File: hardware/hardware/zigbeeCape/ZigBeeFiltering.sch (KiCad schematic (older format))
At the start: 33 parts, among them U2 0.8Ghz_and_2.4GHz_Filter, U3 SMA_Antenna

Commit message: Completed BOM except unlabled DNM parts, labled in red. Completed footprint association except onboard antenae
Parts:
- AE1: footprint Connector_Coaxial:SMA_Amphenol_132134-16_Vertical -> (none)
- L10, L13, L3, L4, L7: footprint (none) -> Inductor_SMD:L_0402_1005Metric_Pad0.77x0.64mm_HandSolder
- L11, L12, L14, L5, L6, L8, L9: footprint (none) -> Inductor_SMD:L_0603_1608Metric_Pad1.05x0.95mm_HandSolder
- L2: footprint (none) -> Inductor_SMD:L_0805_2012Metric_Pad1.15x1.40mm_HandSolder
- U2: footprint (none) -> zigbeeCape:DPX252690DT-5032B1
- U3: footprint (none) -> Connector_Coaxial:SMA_Amphenol_132134-16_Vertical
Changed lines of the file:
@@
 F 0 "L5" H 2253 4946 50  0000 L CNN
 F 1 "3.9nH" H 2253 4855 50  0000 L CNN
-F 2 "" H 2200 4900 50  0001 C CNN
+F 2 "Inductor_SMD:L_0603_1608Metric_Pad1.05x0.95mm_HandSolder" H 2200 4900 50  0001 C CNN
 F 3 "~" H 2200 4900 50  0001 C CNN
 	1    2200 4900
@@
 F 0 "L6" H 2253 5346 50  0000 L CNN
 F 1 "3.9nH" H 2253 5255 50  0000 L CNN
-F 2 "" H 2200 5300 50  0001 C CNN
+F 2 "Inductor_SMD:L_0603_1608Metric_Pad1.05x0.95mm_HandSolder" H 2200 5300 50  0001 C CNN
 F 3 "~" H 2200 5300 50  0001 C CNN
 	1    2200 5300
@@
 F 0 "L9" H 3053 4696 50  0000 L CNN
 F 1 "10nH" H 3053 4605 50  0000 L CNN
-F 2 "" H 3000 4650 50  0001 C CNN
+F 2 "Inductor_SMD:L_0603_1608Metric_Pad1.05x0.95mm_HandSolder" H 3000 4650 50  0001 C CNN
 F 3 "~" H 3000 4650 50  0001 C CNN
 	1    3000 4650
@@
 F 0 "L12" H 4603 5146 50  0000 L CNN
 F 1 "9.1nH" H 4603 5055 50  0000 L CNN
-F 2 "" H 4550 5100 50  0001 C CNN
+F 2 "Inductor_SMD:L_0603_1608Metric_Pad1.05x0.95mm_HandSolder" H 4550 5100 50  0001 C CNN
 F 3 "~" H 4550 5100 50  0001 C CNN
 	1    4550 5100
@@
 F 0 "L11" H 3453 5346 50  0000 L CNN
 F 1 "10nH" H 3453 5255 50  0000 L CNN
-F 2 "" H 3400 5300 50  0001 C CNN
+F 2 "Inductor_SMD:L_0603_1608Metric_Pad1.05x0.95mm_HandSolder" H 3400 5300 50  0001 C CNN
 F 3 "~" H 3400 5300 50  0001 C CNN
 	1    3400 5300
@@
 F 0 "L8" H 2903 5146 50  0000 L CNN
 F 1 "22nH" H 2903 5055 50  0000 L CNN
-F 2 "" H 2850 5100 50  0001 C CNN
+F 2 "Inductor_SMD:L_0603_1608Metric_Pad1.05x0.95mm_HandSolder" H 2850 5100 50  0001 C CNN
 F 3 "~" H 2850 5100 50  0001 C CNN
 	1    2850 5100
@@
 F 0 "U3" H 7800 3815 50  0000 C CNN
 F 1 "SMA_Antenna" H 7800 3724 50  0000 C CNN
-F 2 "" H 7800 3000 50  0001 C CNN
+F 2 "Connector_Coaxial:SMA_Amphenol_132134-16_Vertical" H 7800 3000 50  0001 C CNN
 F 3 "" H 7800 3000 50  0001 C CNN
 	1    7800 3450
@@
 F 0 "L7" H 3403 3246 50  0000 L CNN
 F 1 "2nH" H 3403 3155 50  0000 L CNN
-F 2 "" H 3350 3200 50  0001 C CNN
+F 2 "Inductor_SMD:L_0402_1005Metric_Pad0.77x0.64mm_HandSolder" H 3350 3200 50  0001 C CNN
 F 3 "~" H 3350 3200 50  0001 C CNN
 	1    3350 3200
@@
 F 0 "L10" H 4103 3246 50  0000 L CNN
 F 1 "2nH" H 4103 3155 50  0000 L CNN
-F 2 "" H 4050 3200 50  0001 C CNN
+F 2 "Inductor_SMD:L_0402_1005Metric_Pad0.77x0.64mm_HandSolder" H 4050 3200 50  0001 C CNN
 F 3 "~" H 4050 3200 50  0001 C CNN
 	1    4050 3200
@@
 F 0 "L3" H 2553 2746 50  0000 L CNN
 F 1 "2.4nH" H 2553 2655 50  0000 L CNN
-F 2 "" H 2500 2700 50  0001 C CNN
+F 2 "Inductor_SMD:L_0402_1005Metric_Pad0.77x0.64mm_HandSolder" H 2500 2700 50  0001 C CNN
 F 3 "~" H 2500 2700 50  0001 C CNN
 	1    2500 2700
@@
 F 0 "L4" H 2953 3546 50  0000 L CNN
 F 1 "2.4nH" H 2953 3455 50  0000 L CNN
-F 2 "" H 2900 3500 50  0001 C CNN
+F 2 "Inductor_SMD:L_0402_1005Metric_Pad0.77x0.64mm_HandSolder" H 2900 3500 50  0001 C CNN
 F 3 "~" H 2900 3500 50  0001 C CNN
 	1    2900 3500
@@
 F 0 "L2" H 2353 3296 50  0000 L CNN
 F 1 "15nH" H 2353 3205 50  0000 L CNN
-F 2 "" H 2300 3250 50  0001 C CNN
+F 2 "Inductor_SMD:L_0805_2012Metric_Pad1.15x1.40mm_HandSolder" H 2300 3250 50  0001 C CNN
 F 3 "~" H 2300 3250 50  0001 C CNN
 	1    2300 3250
@@
 F 0 "L13" V 8390 4250 50  0000 C CNN
 F 1 "3.3nH" V 8299 4250 50  0000 C CNN
-F 2 "" H 8200 4250 50  0001 C CNN
+F 2 "Inductor_SMD:L_0402_1005Metric_Pad0.77x0.64mm_HandSolder" H 8200 4250 50  0001 C CNN
 F 3 "~" H 8200 4250 50  0001 C CNN
 	1    8200 4250
@@
 F 0 "L14" H 9052 4546 50  0000 L CNN
 F 1 "DNM" H 9052 4455 50  0000 L CNN
-F 2 "" H 9000 4500 50  0001 C CNN
+F 2 "Inductor_SMD:L_0603_1608Metric_Pad1.05x0.95mm_HandSolder" H 9000 4500 50  0001 C CNN
 F 3 "~" H 9000 4500 50  0001 C CNN
 	1    9000 4500
@@
 F 0 "AE1" H 9780 3989 50  0000 L CNN
 F 1 "Antenna" H 9780 3898 50  0000 L CNN
-F 2 "Connector_Coaxial:SMA_Amphenol_132134-16_Vertical" H 9700 4000 50  0001 C CNN
+F 2 "" H 9700 4000 50  0001 C CNN
 F 3 "~" H 9700 4000 50  0001 C CNN
 	1    9700 4000
@@
 F 0 "U2" H 6150 4625 50  0000 C CNN
 F 1 "0.8Ghz_and_2.4GHz_Filter" H 6150 4534 50  0000 C CNN
-F 2 "" H 6200 4150 50  0001 C CNN
+F 2 "zigbeeCape:DPX252690DT-5032B1" H 6200 4150 50  0001 C CNN
 F 3 "" H 6200 4150 50  0001 C CNN
 	1    6300 4150

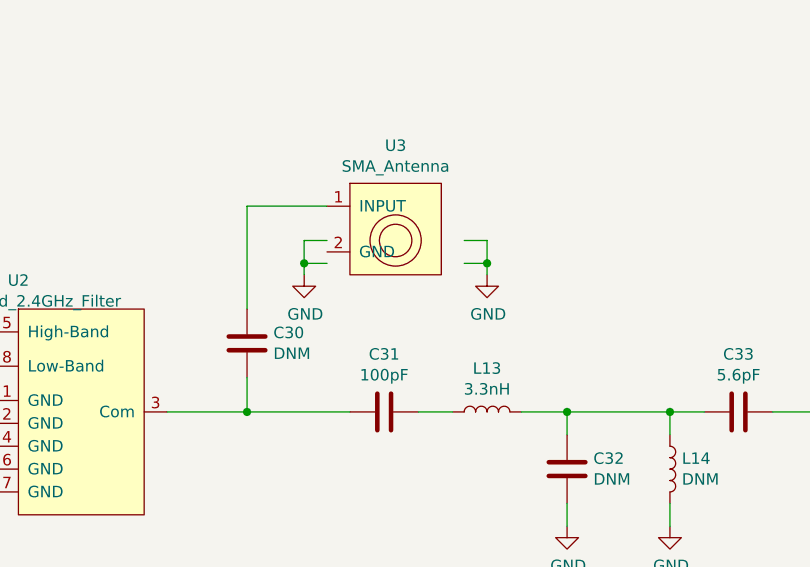
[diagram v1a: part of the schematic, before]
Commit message: Setup DRC, completed coms lines
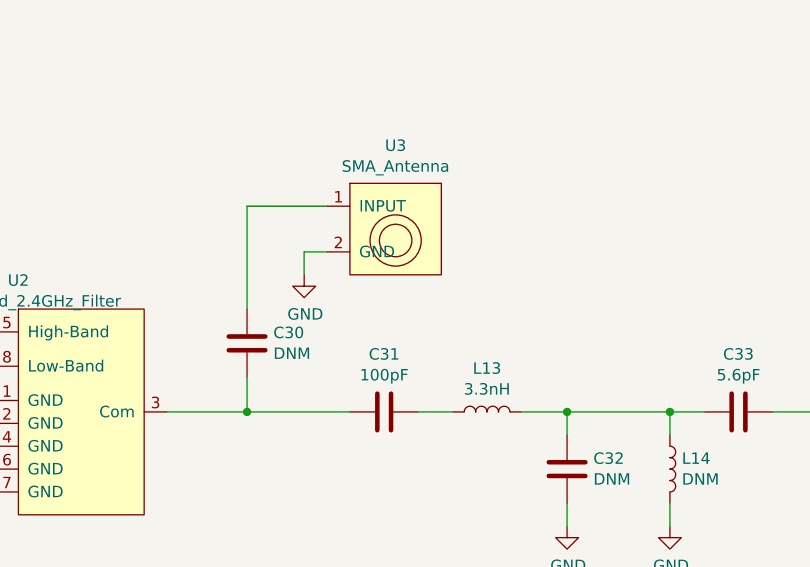
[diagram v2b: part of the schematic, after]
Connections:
- wire segments 104 -> 98
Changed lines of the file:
@@
 	1    0    0    -1
 $EndComp
-$Comp
-L power:GND #PWR043
-U 1 1 608A9A63
-P 8200 3650
-F 0 "#PWR043" H 8200 3400 50  0001 C CNN
-F 1 "GND" H 8205 3477 50  0000 C CNN
-F 2 "" H 8200 3650 50  0001 C CNN
-F 3 "" H 8200 3650 50  0001 C CNN
-	1    8200 3650
-	1    0    0    -1
-$EndComp
-Wire Wire Line
-	7500 3600 7400 3600
-Wire Wire Line
-	7400 3600 7400 3650
-Wire Wire Line
-	7400 3600 7400 3500
-Wire Wire Line
-	7400 3500 7500 3500
-Connection ~ 7400 3600
-Wire Wire Line
-	8100 3500 8200 3500
-Wire Wire Line
-	8200 3500 8200 3600
-Wire Wire Line
-	8100 3600 8200 3600
-Connection ~ 8200 3600
-Wire Wire Line
-	8200 3600 8200 3650
 Wire Wire Line
 	7900 4250 8050 4250
@@
 	6800 4250 7150 4250
 Connection ~ 7150 4250
+Wire Wire Line
+	7400 3650 7400 3550
+Wire Wire Line
+	7400 3550 7500 3550
 $EndSCHEMATC

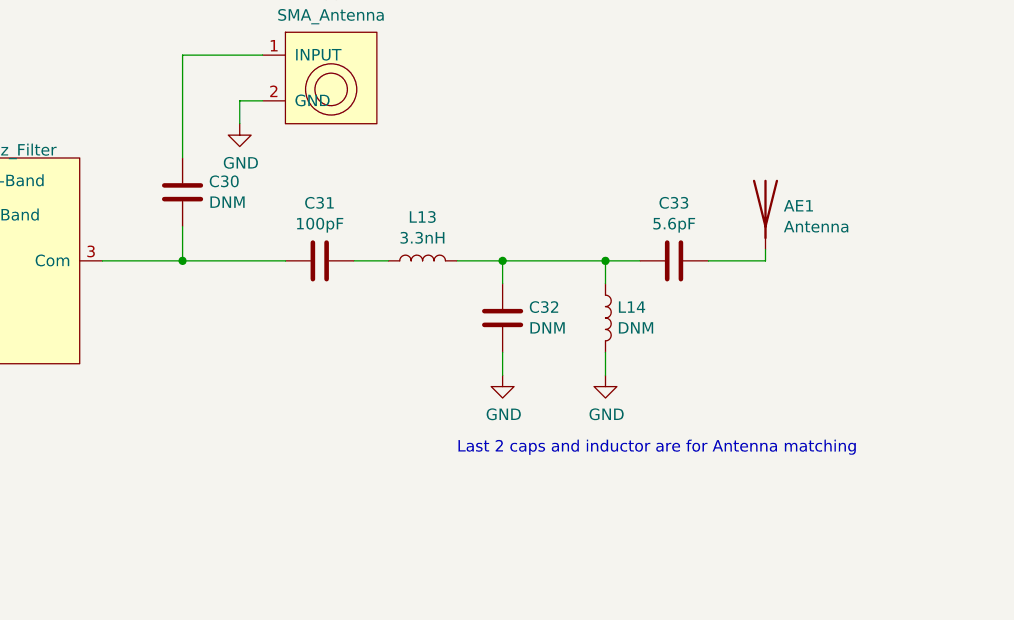
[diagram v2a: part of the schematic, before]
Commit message: Finished ZigBee circuit, Removed PCB antenna
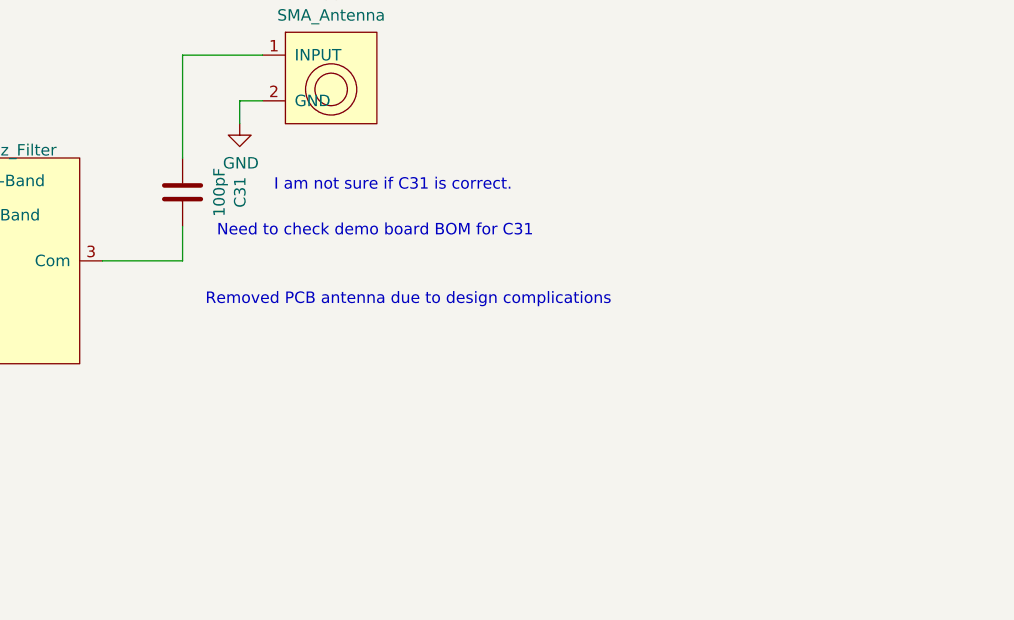
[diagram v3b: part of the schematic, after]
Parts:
- removed AE1: Antenna, symbol Device:Antenna
- removed C30, C32: DNM, Capacitor_SMD:C_0603_1608Metric_Pad1.08x0.95mm_HandSolder, symbol Device:C
- removed C33: 5.6pF, Capacitor_SMD:C_0603_1608Metric_Pad1.08x0.95mm_HandSolder, symbol Device:C
- removed L13: 3.3nH, Inductor_SMD:L_0402_1005Metric_Pad0.77x0.64mm_HandSolder, symbol Device:L
- removed L14: DNM, Inductor_SMD:L_0603_1608Metric_Pad1.05x0.95mm_HandSolder, symbol Device:L
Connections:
- net at U3.1 (INPUT): now also C31.2
- net at C31.1: now also U2.3 (Com)
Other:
- note added: "I am not sure if C31 is correct."
- note added: "Need to check demo board BOM for C31"
- note added: "Removed PCB antenna due to design complications"
- note removed: "Last 2 caps and inductor are for Antenna matching\n"
- moved on the sheet: C31
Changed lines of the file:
@@
 Wire Wire Line
 	4550 3650 4550 3750
-$Comp
-L Device:C C31
-U 1 1 608925A4
-P 7750 4250
-F 0 "C31" V 7498 4250 50  0000 C CNN
-F 1 "100pF" V 7589 4250 50  0000 C CNN
-F 2 "Capacitor_SMD:C_0603_1608Metric_Pad1.08x0.95mm_HandSolder" H 7788 4100 50  0001 C CNN
-F 3 "~" H 7750 4250 50  0001 C CNN
-	1    7750 4250
-	0    1    1    0
-$EndComp
-$Comp
-L Device:C C30
-U 1 1 60892E78
-P 7150 3950
-F 0 "C30" H 7265 3996 50  0000 L CNN
-F 1 "DNM" H 7265 3905 50  0000 L CNN
-F 2 "Capacitor_SMD:C_0603_1608Metric_Pad1.08x0.95mm_HandSolder" H 7188 3800 50  0001 C CNN
-F 3 "~" H 7150 3950 50  0001 C CNN
-	1    7150 3950
-	1    0    0    -1
-$EndComp
-$Comp
-L Device:L L13
-U 1 1 6089332B
-P 8200 4250
-F 0 "L13" V 8390 4250 50  0000 C CNN
-F 1 "3.3nH" V 8299 4250 50  0000 C CNN
-F 2 "Inductor_SMD:L_0402_1005Metric_Pad0.77x0.64mm_HandSolder" H 8200 4250 50  0001 C CNN
-F 3 "~" H 8200 4250 50  0001 C CNN
-	1    8200 4250
-	0    -1   -1   0
-$EndComp
-$Comp
-L Device:L L14
-U 1 1 6089391E
-P 9000 4500
-F 0 "L14" H 9052 4546 50  0000 L CNN
-F 1 "DNM" H 9052 4455 50  0000 L CNN
-F 2 "Inductor_SMD:L_0603_1608Metric_Pad1.05x0.95mm_HandSolder" H 9000 4500 50  0001 C CNN
-F 3 "~" H 9000 4500 50  0001 C CNN
-	1    9000 4500
-	1    0    0    -1
-$EndComp
-$Comp
-L Device:C C32
-U 1 1 608951FF
-P 8550 4500
-F 0 "C32" H 8665 4546 50  0000 L CNN
-F 1 "DNM" H 8665 4455 50  0000 L CNN
-F 2 "Capacitor_SMD:C_0603_1608Metric_Pad1.08x0.95mm_HandSolder" H 8588 4350 50  0001 C CNN
-F 3 "~" H 8550 4500 50  0001 C CNN
-	1    8550 4500
-	1    0    0    -1
-$EndComp
-$Comp
-L Device:C C33
-U 1 1 608A5A12
-P 9300 4250
-F 0 "C33" V 9552 4250 50  0000 C CNN
-F 1 "5.6pF" V 9461 4250 50  0000 C CNN
-F 2 "Capacitor_SMD:C_0603_1608Metric_Pad1.08x0.95mm_HandSolder" H 9338 4100 50  0001 C CNN
-F 3 "~" H 9300 4250 50  0001 C CNN
-	1    9300 4250
-	0    -1   -1   0
-$EndComp
 Wire Wire Line
 	7150 3800 7150 3350
@@
 	1    0    0    -1
 $EndComp
-Wire Wire Line
-	7900 4250 8050 4250
-Wire Wire Line
-	8350 4250 8550 4250
-Wire Wire Line
-	8550 4250 8550 4350
-Wire Wire Line
-	8550 4250 9000 4250
-Wire Wire Line
-	9000 4250 9000 4350
-Connection ~ 8550 4250
-Wire Wire Line
-	9000 4250 9150 4250
-Connection ~ 9000 4250
-$Comp
-L power:GND #PWR044
-U 1 1 608BE07F
-P 8550 4750
-F 0 "#PWR044" H 8550 4500 50  0001 C CNN
-F 1 "GND" H 8555 4577 50  0000 C CNN
-F 2 "" H 8550 4750 50  0001 C CNN
-F 3 "" H 8550 4750 50  0001 C CNN
-	1    8550 4750
-	1    0    0    -1
-$EndComp
-$Comp
-L power:GND #PWR045
-U 1 1 608C0318
-P 9000 4750
-F 0 "#PWR045" H 9000 4500 50  0001 C CNN
-F 1 "GND" H 9005 4577 50  0000 C CNN
-F 2 "" H 9000 4750 50  0001 C CNN
-F 3 "" H 9000 4750 50  0001 C CNN
-	1    9000 4750
-	1    0    0    -1
-$EndComp
-Wire Wire Line
-	8550 4650 8550 4750
-Wire Wire Line
-	9000 4650 9000 4750
-$Comp
-L Device:Antenna AE1
-U 1 1 608C74F4
-P 9700 4000
-F 0 "AE1" H 9780 3989 50  0000 L CNN
-F 1 "Antenna" H 9780 3898 50  0000 L CNN
-F 2 "" H 9700 4000 50  0001 C CNN
-F 3 "~" H 9700 4000 50  0001 C CNN
-	1    9700 4000
-	1    0    0    -1
-$EndComp
-Wire Wire Line
-	9450 4250 9700 4250
-Wire Wire Line
-	9700 4250 9700 4200
-Text Notes 8350 5100 0    50   ~ 0
-Last 2 caps and inductor are for Antenna matching\n
-Wire Wire Line
-	7150 4250 7600 4250
 Wire Wire Line
 	7150 4100 7150 4250
@@
 Wire Wire Line
 	6800 4250 7150 4250
-Connection ~ 7150 4250
 Wire Wire Line
 	7400 3650 7400 3550
 Wire Wire Line
 	7400 3550 7500 3550
+$Comp
+L Device:C C31
+U 1 1 608925A4
+P 7150 3950
+F 0 "C31" V 6898 3950 50  0000 C CNN
+F 1 "100pF" V 6989 3950 50  0000 C CNN
+F 2 "Capacitor_SMD:C_0603_1608Metric_Pad1.08x0.95mm_HandSolder" H 7188 3800 50  0001 C CNN
+F 3 "~" H 7150 3950 50  0001 C CNN
+	1    7150 3950
+	-1   0    0    1
+$EndComp
+Text Notes 7550 3950 0    50   ~ 0
+I am not sure if C31 is correct.
+Text Notes 7250 4450 0    50   ~ 0
+Removed PCB antenna due to design complications
+Text Notes 7300 4150 0    50   ~ 0
+Need to check demo board BOM for C31
 $EndSCHEMATC

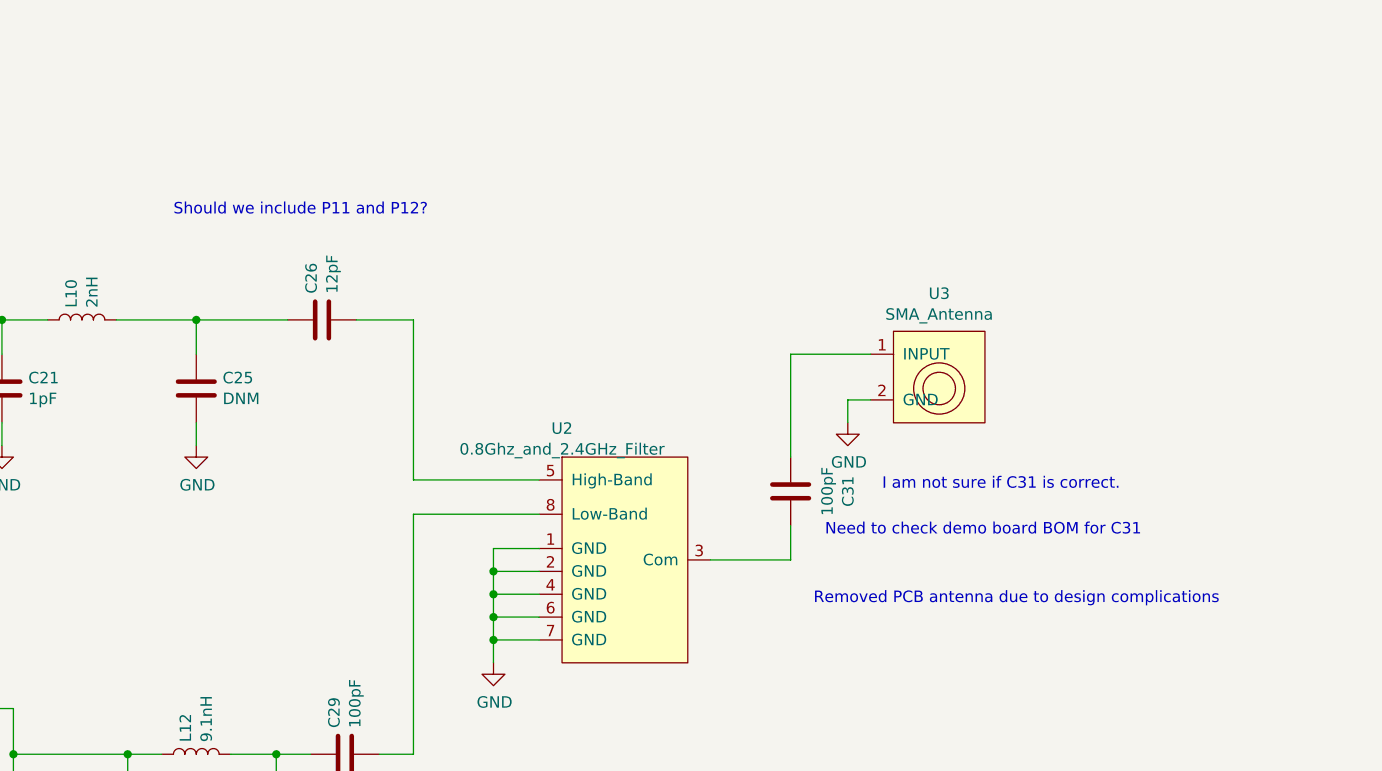
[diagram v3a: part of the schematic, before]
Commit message: Post layout review 1 changes
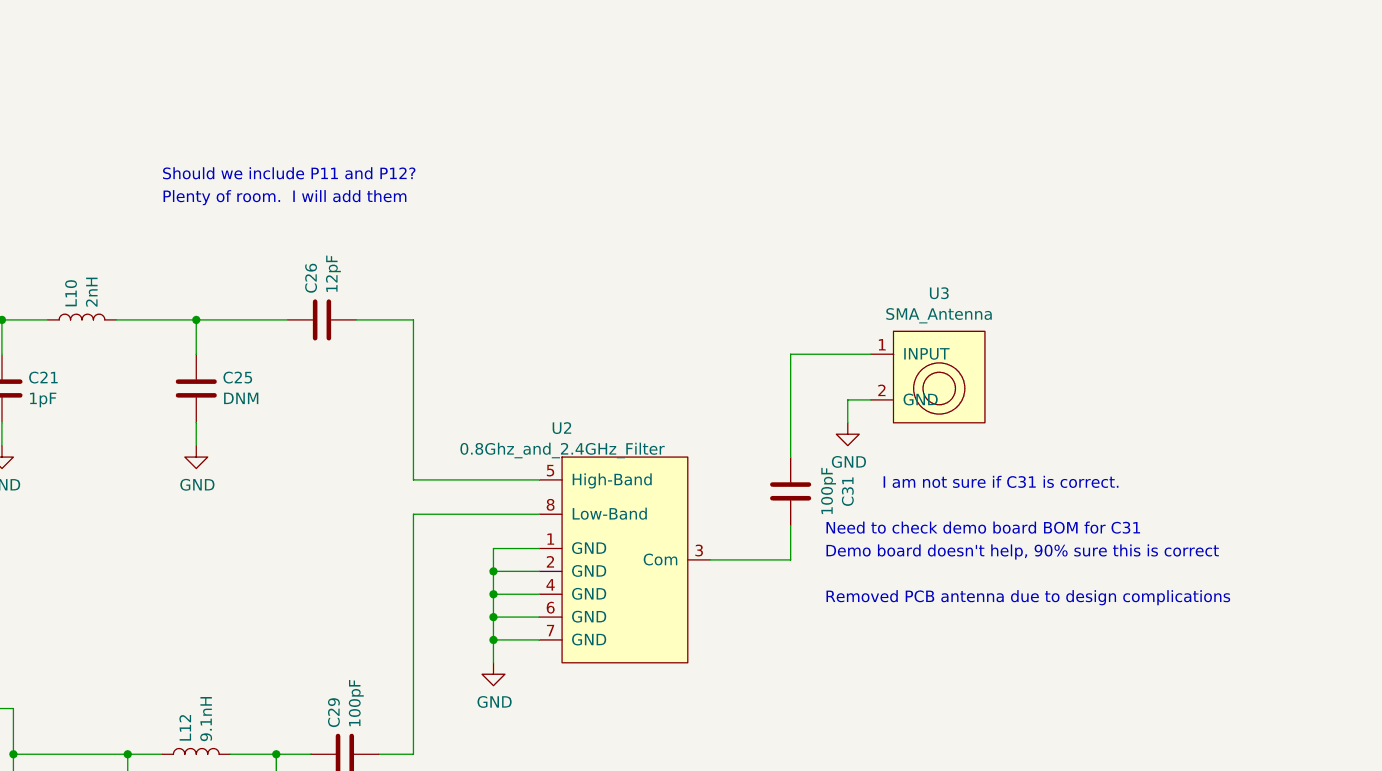
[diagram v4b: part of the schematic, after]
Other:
- note added: "Demo board doesn't help, 90% sure this is correct"
- note added: "Plenty of room. I will add them"
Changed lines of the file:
@@
 Wire Wire Line
 	7150 4100 7150 4250
-Text Notes 4450 2750 0    50   ~ 0
+Text Notes 4400 2600 0    50   ~ 0
 Should we include P11 and P12?
 Text HLabel 2150 3000 0    50   Input ~ 0
@@
 Text Notes 7550 3950 0    50   ~ 0
 I am not sure if C31 is correct.
-Text Notes 7250 4450 0    50   ~ 0
+Text Notes 7300 4450 0    50   ~ 0
 Removed PCB antenna due to design complications
 Text Notes 7300 4150 0    50   ~ 0
 Need to check demo board BOM for C31
+Text Notes 7300 4250 0    50   ~ 0
+Demo board doesn't help, 90% sure this is correct
+Text Notes 4400 2700 0    50   ~ 0
+Plenty of room.  I will add them
 $EndSCHEMATC
